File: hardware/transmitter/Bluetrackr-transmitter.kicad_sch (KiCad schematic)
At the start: 57 parts, among them J1 USB_C_Receptacle_USB2.0, J2 Programming_Connector, J3 Battery_Connector, Q1 CJ2333, Q2 BSS138, Q3 BSS138, Q4 BSS138, Q5 BSS138, Q6 BSS138, SW1 SW_Pair, U1 MCP73831-2-OT, U2 MIC5205-3.3YM5, U3 MCP1700-1802E_SOT23, U4 STM32F030R8Tx, U5 NRF24L01_Breakout, U6 ICM-20948

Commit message: Change level shifting resistors to 10k
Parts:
- R10, R11, R12, R13, R14, R15, R16, R17, R18, R19: value 2.2k -> 10k
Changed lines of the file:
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@@
   (junction (at 359.41 142.24))
   (junction (at 359.41 173.99))
+  (no_connect (at 217.17 148.59))
+  (no_connect (at 247.65 176.53))
+  (no_connect (at 217.17 186.69))
+  (no_connect (at 217.17 181.61))
+  (no_connect (at 54.61 73.66))
+  (no_connect (at 247.65 138.43))
+  (no_connect (at 217.17 194.31))
+  (no_connect (at 247.65 186.69))
+  (no_connect (at 54.61 60.96))
+  (no_connect (at 247.65 143.51))
+  (no_connect (at 325.12 57.15))
+  (no_connect (at 247.65 156.21))
+  (no_connect (at 217.17 196.85))
+  (no_connect (at 247.65 166.37))
+  (no_connect (at 247.65 140.97))
+  (no_connect (at 217.17 173.99))
+  (no_connect (at 217.17 168.91))
+  (no_connect (at 217.17 199.39))
+  (no_connect (at 247.65 148.59))
+  (no_connect (at 217.17 184.15))
   (no_connect (at 247.65 161.29))
+  (no_connect (at 325.12 54.61))
+  (no_connect (at 247.65 146.05))
+  (no_connect (at 217.17 138.43))
+  (no_connect (at 247.65 171.45))
+  (no_connect (at 217.17 179.07))
+  (no_connect (at 54.61 63.5))
+  (no_connect (at 217.17 156.21))
+  (no_connect (at 299.72 62.23))
+  (no_connect (at 217.17 143.51))
+  (no_connect (at 217.17 140.97))
+  (no_connect (at 247.65 184.15))
+  (no_connect (at 247.65 181.61))
+  (no_connect (at 247.65 168.91))
+  (no_connect (at 247.65 123.19))
+  (no_connect (at 247.65 179.07))
+  (no_connect (at 217.17 189.23))
+  (no_connect (at 54.61 58.42))
+  (no_connect (at 247.65 125.73))
+  (no_connect (at 247.65 173.99))
+  (no_connect (at 217.17 151.13))
+  (no_connect (at 247.65 163.83))
   (no_connect (at 217.17 191.77))
-  (no_connect (at 247.65 163.83))
-  (no_connect (at 299.72 62.23))
-  (no_connect (at 54.61 63.5))
-  (no_connect (at 247.65 156.21))
-  (no_connect (at 217.17 181.61))
-  (no_connect (at 247.65 184.15))
-  (no_connect (at 247.65 123.19))
-  (no_connect (at 54.61 60.96))
-  (no_connect (at 325.12 57.15))
-  (no_connect (at 217.17 140.97))
-  (no_connect (at 247.65 181.61))
-  (no_connect (at 217.17 184.15))
+  (no_connect (at 247.65 189.23))
   (no_connect (at 54.61 66.04))
-  (no_connect (at 247.65 166.37))
-  (no_connect (at 247.65 138.43))
-  (no_connect (at 247.65 143.51))
-  (no_connect (at 247.65 186.69))
-  (no_connect (at 247.65 140.97))
-  (no_connect (at 217.17 196.85))
-  (no_connect (at 54.61 73.66))
-  (no_connect (at 217.17 148.59))
-  (no_connect (at 217.17 186.69))
-  (no_connect (at 247.65 148.59))
-  (no_connect (at 217.17 156.21))
   (no_connect (at 54.61 76.2))
-  (no_connect (at 247.65 173.99))
-  (no_connect (at 247.65 176.53))
-  (no_connect (at 217.17 173.99))
-  (no_connect (at 217.17 199.39))
-  (no_connect (at 247.65 125.73))
-  (no_connect (at 247.65 171.45))
-  (no_connect (at 217.17 143.51))
-  (no_connect (at 217.17 189.23))
-  (no_connect (at 247.65 146.05))
-  (no_connect (at 217.17 179.07))
-  (no_connect (at 217.17 168.91))
-  (no_connect (at 247.65 189.23))
-  (no_connect (at 325.12 54.61))
-  (no_connect (at 217.17 138.43))
-  (no_connect (at 247.65 168.91))
-  (no_connect (at 247.65 179.07))
-  (no_connect (at 217.17 194.31))
-  (no_connect (at 54.61 58.42))
-  (no_connect (at 217.17 151.13))
   (wire (pts (xy 31.75 83.82) (xy 31.75 86.36))
     (stroke (width 0) (type solid) (color 0 0 0 0))
@@
       (effects (font (size 1.27 1.27)) (justify left))
     )
-    (property "Value" "2.2k" (id 1) (at 300.228 137.033 0)
+    (property "Value" "10k" (id 1) (at 300.228 137.033 0)
       (effects (font (size 1.27 1.27)) (justify left))
     )
@@
       (effects (font (size 1.27 1.27)) (justify left))
     )
-    (property "Value" "2.2k" (id 1) (at 300.228 168.783 0)
+    (property "Value" "10k" (id 1) (at 300.228 168.783 0)
       (effects (font (size 1.27 1.27)) (justify left))
     )
@@
       (effects (font (size 1.27 1.27)) (justify left))
     )
-    (property "Value" "2.2k" (id 1) (at 315.468 137.033 0)
+    (property "Value" "10k" (id 1) (at 315.468 137.033 0)
       (effects (font (size 1.27 1.27)) (justify left))
     )
@@
       (effects (font (size 1.27 1.27)) (justify left))
     )
-    (property "Value" "2.2k" (id 1) (at 315.468 168.783 0)
+    (property "Value" "10k" (id 1) (at 315.468 168.783 0)
       (effects (font (size 1.27 1.27)) (justify left))
     )
@@
       (effects (font (size 1.27 1.27)) (justify left))
     )
-    (property "Value" "2.2k" (id 1) (at 323.088 105.283 0)
+    (property "Value" "10k" (id 1) (at 323.088 105.283 0)
       (effects (font (size 1.27 1.27)) (justify left))
     )
@@
       (effects (font (size 1.27 1.27)) (justify left))
     )
-    (property "Value" "2.2k" (id 1) (at 338.328 105.283 0)
+    (property "Value" "10k" (id 1) (at 338.328 105.283 0)
       (effects (font (size 1.27 1.27)) (justify left))
     )
@@
       (effects (font (size 1.27 1.27)) (justify left))
     )
-    (property "Value" "2.2k" (id 1) (at 345.948 137.033 0)
+    (property "Value" "10k" (id 1) (at 345.948 137.033 0)
       (effects (font (size 1.27 1.27)) (justify left))
     )
@@
       (effects (font (size 1.27 1.27)) (justify left))
     )
-    (property "Value" "2.2k" (id 1) (at 345.948 168.783 0)
+    (property "Value" "10k" (id 1) (at 345.948 168.783 0)
       (effects (font (size 1.27 1.27)) (justify left))
     )
@@
       (effects (font (size 1.27 1.27)) (justify left))
     )
-    (property "Value" "2.2k" (id 1) (at 361.188 137.033 0)
+    (property "Value" "10k" (id 1) (at 361.188 137.033 0)
       (effects (font (size 1.27 1.27)) (justify left))
     )
@@
       (effects (font (size 1.27 1.27)) (justify left))
     )
-    (property "Value" "2.2k" (id 1) (at 361.188 168.783 0)
-      (effects (font (size 1.27 1.27)) (justify left))
-    )
+    (property "Value" "10k" (id 1) (at 361.188 168.783 0)
+      (effects (font (size 1.27 1.27)) (justify left))
+    )

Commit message: Changed regulator from 3.3V to 2.5V
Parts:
- removed U2: MIC5205-3.3YM5, Package_TO_SOT_SMD:SOT-23-5, symbol Regulator_Linear:MIC5205-3.3YM5
- added U?: MIC5205-2.5YM5, Package_TO_SOT_SMD:SOT-23-5, symbol Regulator_Linear:MIC5205-2.5YM5
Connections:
- net GND: now also U?.2 (GND)
- net VCC: now also U?.1 (IN), U?.3 (EN)
- net at C4.1: now also U?.4 (BP)
- net +3V3 renamed +2V5
- net +2V5: now also U?.5 (OUT)
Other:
- note added: "2.5V"
- note removed: "3.3V"

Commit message: Began routing the pcb
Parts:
- added C1, C3: 4.7u, Capacitor_SMD:C_0805_2012Metric_Pad1.15x1.40mm_HandSolder, symbol Device:C
- J2: footprint Connector_JST:JST_XH_S4B-XH-A_1x04_P2.50mm_Horizontal -> Connector_JST:JST_XH_B4B-XH-A_1x04_P2.50mm_Vertical
- J3: footprint Connector_JST:JST_XH_B2B-XH-A_1x02_P2.50mm_Vertical -> Connector_JST:JST_XH_S2B-XH-A_1x02_P2.50mm_Horizontal
- U5: footprint RF_Module:nRF24L01_Breakout -> Modules:nRF24L01_Breakout
- gave numbers to parts that had none: 1
- renumbered C8 to C10, C9 to C11, C10 to C12, C11 to C13, C12 to C14, C13 to C15, C14 to C16, C15 to C17, C1 to C2, C2 to C4, C3 to C5, C4 to C6, C5 to C7, C6 to C8, C7 to C9
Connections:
- net +BATT: now also C3.1
- net BATT_SENSE: now also U4.57 (PB5); no longer U4.14 (PA0)
- net GND: now also C1.2, C3.2
- net VBUS: now also C1.1
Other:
- moved on the sheet: C4, C5, C6, C7, C8, U2, U3

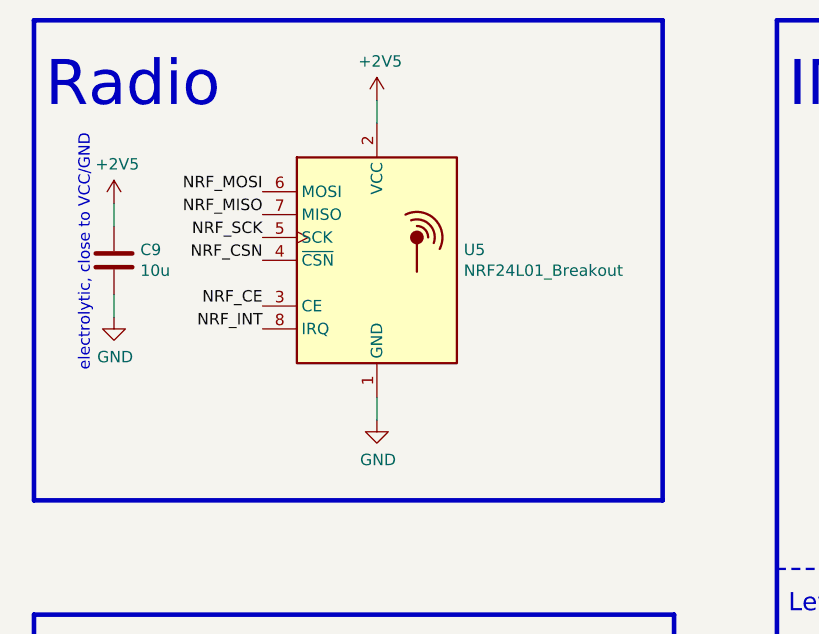
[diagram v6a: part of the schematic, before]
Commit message: Replace nRF24 breakout with DL-24N nRF24 smd module
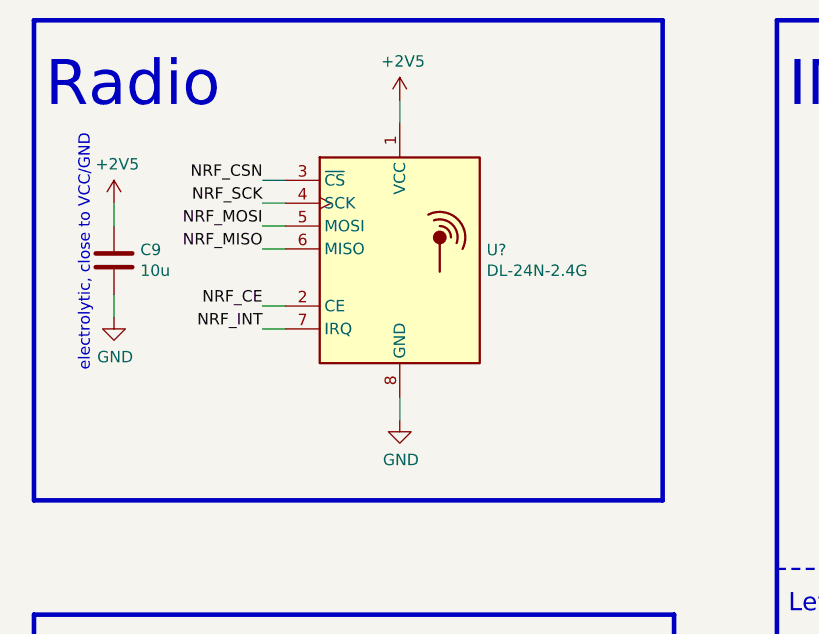
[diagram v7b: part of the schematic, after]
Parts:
- removed U5: NRF24L01_Breakout, Modules:nRF24L01_Breakout, symbol RF:NRF24L01_Breakout
- added U?: DL-24N-2.4G, User_Module:DL-24N-2.4G, symbol User_Module:DL-24N-2.4G
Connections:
- net +2V5: now also U?.1 (VCC)
- net GND: now also U?.8 (GND)
- net NRF_CE: now also U?.2 (CE)
- net NRF_CSN: now also U?.3 (~CS)
- net NRF_INT: now also U?.7 (IRQ)
- net NRF_MISO: now also U?.6 (MISO)
- net NRF_MOSI: now also U?.5 (MOSI)
- net NRF_SCK: now also U?.4 (SCK)
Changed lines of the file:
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@@
-(kicad_sch (version 20200602) (host eeschema "(5.99.0-1899-g8e8979e31)")
+(kicad_sch (version 20200602) (host eeschema "(5.99.0-1933-g2401ed587)")
   (page 1 1)
   (paper "A3")
@@
   (junction (at 359.41 142.24))
   (junction (at 359.41 173.99))
-  (no_connect (at 217.17 148.59))
-  (no_connect (at 54.61 66.04))
-  (no_connect (at 54.61 63.5))
-  (no_connect (at 54.61 60.96))
-  (no_connect (at 217.17 173.99))
-  (no_connect (at 325.12 54.61))
+  (no_connect (at 217.17 168.91))
+  (no_connect (at 325.12 57.15))
   (no_connect (at 247.65 166.37))
   (no_connect (at 217.17 196.85))
-  (no_connect (at 247.65 118.11))
-  (no_connect (at 217.17 199.39))
-  (no_connect (at 325.12 57.15))
+  (no_connect (at 247.65 140.97))
+  (no_connect (at 325.12 54.61))
+  (no_connect (at 54.61 60.96))
+  (no_connect (at 54.61 73.66))
   (no_connect (at 247.65 161.29))
-  (no_connect (at 217.17 191.77))
-  (no_connect (at 217.17 184.15))
+  (no_connect (at 247.65 184.15))
+  (no_connect (at 217.17 189.23))
   (no_connect (at 247.65 143.51))
-  (no_connect (at 247.65 163.83))
+  (no_connect (at 54.61 63.5))
+  (no_connect (at 217.17 156.21))
+  (no_connect (at 247.65 171.45))
   (no_connect (at 247.65 138.43))
-  (no_connect (at 247.65 123.19))
-  (no_connect (at 54.61 76.2))
-  (no_connect (at 247.65 184.15))
-  (no_connect (at 217.17 181.61))
-  (no_connect (at 54.61 58.42))
-  (no_connect (at 247.65 140.97))
   (no_connect (at 247.65 148.59))
-  (no_connect (at 217.17 138.43))
-  (no_connect (at 247.65 176.53))
-  (no_connect (at 299.72 62.23))
-  (no_connect (at 247.65 125.73))
-  (no_connect (at 247.65 168.91))
-  (no_connect (at 217.17 189.23))
+  (no_connect (at 217.17 194.31))
   (no_connect (at 247.65 146.05))
-  (no_connect (at 217.17 186.69))
-  (no_connect (at 247.65 171.45))
-  (no_connect (at 247.65 189.23))
-  (no_connect (at 217.17 168.91))
   (no_connect (at 247.65 179.07))
+  (no_connect (at 217.17 173.99))
+  (no_connect (at 299.72 62.23))
+  (no_connect (at 54.61 76.2))
+  (no_connect (at 217.17 140.97))
+  (no_connect (at 217.17 143.51))
+  (no_connect (at 217.17 199.39))
+  (no_connect (at 217.17 148.59))
+  (no_connect (at 247.65 176.53))
+  (no_connect (at 54.61 66.04))
+  (no_connect (at 247.65 189.23))
+  (no_connect (at 247.65 123.19))
+  (no_connect (at 217.17 191.77))
+  (no_connect (at 217.17 138.43))
+  (no_connect (at 217.17 181.61))
   (no_connect (at 217.17 179.07))
-  (no_connect (at 217.17 156.21))
-  (no_connect (at 247.65 156.21))
-  (no_connect (at 247.65 186.69))
+  (no_connect (at 247.65 118.11))
+  (no_connect (at 247.65 163.83))
+  (no_connect (at 217.17 184.15))
+  (no_connect (at 217.17 186.69))
   (no_connect (at 217.17 151.13))
+  (no_connect (at 247.65 168.91))
+  (no_connect (at 247.65 186.69))
   (no_connect (at 247.65 181.61))
-  (no_connect (at 217.17 140.97))
-  (no_connect (at 54.61 73.66))
-  (no_connect (at 217.17 143.51))
-  (no_connect (at 217.17 194.31))
+  (no_connect (at 54.61 58.42))
+  (no_connect (at 247.65 125.73))
+  (no_connect (at 247.65 156.21))
   (wire (pts (xy 31.75 83.82) (xy 31.75 86.36))
     (stroke (width 0) (type solid) (color 0 0 0 0))
@@
     (stroke (width 0) (type solid) (color 0 0 0 0))
   )
+  (wire (pts (xy 220.98 43.18) (xy 223.52 43.18))
+    (stroke (width 0) (type solid) (color 0 0 0 0))
+  )
+  (wire (pts (xy 220.98 45.72) (xy 223.52 45.72))
+    (stroke (width 0) (type solid) (color 0 0 0 0))
+  )
+  (wire (pts (xy 220.98 48.26) (xy 223.52 48.26))
+    (stroke (width 0) (type solid) (color 0 0 0 0))
+  )
+  (wire (pts (xy 220.98 50.8) (xy 223.52 50.8))
+    (stroke (width 0) (type solid) (color 0 0 0 0))
+  )
+  (wire (pts (xy 220.98 57.15) (xy 223.52 57.15))
+    (stroke (width 0) (type solid) (color 0 0 0 0))
+  )
+  (wire (pts (xy 220.98 59.69) (xy 223.52 59.69))
+    (stroke (width 0) (type solid) (color 0 0 0 0))
+  )
   (wire (pts (xy 229.87 107.95) (xy 229.87 110.49))
     (stroke (width 0) (type solid) (color 0 0 0 0))
@@
     (stroke (width 0) (type solid) (color 0 0 0 0))
   )
-  (wire (pts (xy 233.68 34.29) (xy 233.68 36.83))
-    (stroke (width 0) (type solid) (color 0 0 0 0))
-  )
-  (wire (pts (xy 233.68 67.31) (xy 233.68 69.85))
-    (stroke (width 0) (type solid) (color 0 0 0 0))
-  )
   (wire (pts (xy 234.95 110.49) (xy 232.41 110.49))
     (stroke (width 0) (type solid) (color 0 0 0 0))
@@
     (stroke (width 0) (type solid) (color 0 0 0 0))
   )
+  (wire (pts (xy 236.22 34.29) (xy 236.22 36.83))
+    (stroke (width 0) (type solid) (color 0 0 0 0))
+  )
+  (wire (pts (xy 236.22 67.31) (xy 236.22 69.85))
+    (stroke (width 0) (type solid) (color 0 0 0 0))
+  )
   (wire (pts (xy 237.49 110.49) (xy 234.95 110.49))
     (stroke (width 0) (type solid) (color 0 0 0 0))
@@
     (effects (font (size 1.27 1.27)) (justify right bottom))
   )
-  (label "NRF_MOSI" (at 220.98 44.45 180)
+  (label "NRF_CSN" (at 220.98 43.18 180)
     (effects (font (size 1.27 1.27)) (justify right bottom))
   )
-  (label "NRF_MISO" (at 220.98 46.99 180)
+  (label "NRF_SCK" (at 220.98 45.72 180)
     (effects (font (size 1.27 1.27)) (justify right bottom))
   )
-  (label "NRF_SCK" (at 220.98 49.53 180)
+  (label "NRF_MOSI" (at 220.98 48.26 180)
     (effects (font (size 1.27 1.27)) (justify right bottom))
   )
-  (label "NRF_CSN" (at 220.98 52.07 180)
+  (label "NRF_MISO" (at 220.98 50.8 180)
     (effects (font (size 1.27 1.27)) (justify right bottom))
   )
@@
     )
   )
-  (symbol (lib_id "power:+2V5") (at 233.68 34.29 0) (unit 1)
+  (symbol (lib_id "power:+2V5") (at 236.22 34.29 0) (unit 1)
     (in_bom yes)
-    (property "Reference" "#PWR042" (id 0) (at 233.68 38.1 0)
+    (property "Reference" "#PWR042" (id 0) (at 236.22 38.1 0)
       (effects (font (size 1.27 1.27)) hide)
     )
-    (property "Value" "+2V5" (id 1) (at 234.0483 29.9656 0))
-    (property "Footprint" "" (id 2) (at 233.68 34.29 0)
+    (property "Value" "+2V5" (id 1) (at 236.5883 29.9656 0))
+    (property "Footprint" "" (id 2) (at 236.22 34.29 0)
       (effects (font (size 1.27 1.27)) hide)
     )
-    (property "Datasheet" "" (id 3) (at 233.68 34.29 0)
+    (property "Datasheet" "" (id 3) (at 236.22 34.29 0)
       (effects (font (size 1.27 1.27)) hide)
     )
@@
     )
   )
-  (symbol (lib_id "power:GND") (at 233.68 69.85 0) (unit 1)
+  (symbol (lib_id "power:GND") (at 236.22 69.85 0) (unit 1)
     (in_bom yes)
-    (property "Reference" "#PWR043" (id 0) (at 233.68 76.2 0)
+    (property "Reference" "#PWR043" (id 0) (at 236.22 76.2 0)
       (effects (font (size 1.27 1.27)) hide)
     )
-    (property "Value" "GND" (id 1) (at 233.807 74.2442 0))
-    (property "Footprint" "" (id 2) (at 233.68 69.85 0)
+    (property "Value" "GND" (id 1) (at 236.347 74.2442 0))
+    (property "Footprint" "" (id 2) (at 236.22 69.85 0)
       (effects (font (size 1.27 1.27)) hide)
     )
-    (property "Datasheet" "" (id 3) (at 233.68 69.85 0)
+    (property "Datasheet" "" (id 3) (at 236.22 69.85 0)
       (effects (font (size 1.27 1.27)) hide)
     )
@@
     )
   )
-  (symbol (lib_id "RF:NRF24L01_Breakout") (at 233.68 52.07 0) (unit 1)
+  (symbol (lib_id "User_Module:DL-24N-2.4G") (at 236.22 52.07 0) (unit 1)
     (in_bom yes)
-    (property "Reference" "U5" (id 0) (at 243.332 50.9016 0)
+    (property "Reference" "U?" (id 0) (at 245.8721 50.9206 0)
       (effects (font (size 1.27 1.27)) (justify left))
     )
-    (property "Value" "NRF24L01_Breakout" (id 1) (at 243.332 53.213 0)
+    (property "Value" "DL-24N-2.4G" (id 1) (at 245.8721 53.2193 0)
       (effects (font (size 1.27 1.27)) (justify left))
     )
-    (property "Footprint" "Modules:nRF24L01_Breakout" (id 2) (at 237.49 36.83 0)
+    (property "Footprint" "User_Module:DL-24N-2.4G" (id 2) (at 237.49 36.83 0)
       (effects (font (size 1.27 1.27) italic) (justify left) hide)
     )
-    (property "Datasheet" "http://www.nordicsemi.com/eng/content/download/2730/34105/file/nRF24L01_Product_Specification_v2_0.pdf" (id 3) (at 233.68 54.61 0)
+    (property "Datasheet" "https://datasheet.lcsc.com/szlcsc/1912111437_DreamLNK-DL-24N-2-4G_C381181.pdf" (id 3) (at 236.22 53.34 0)
       (effects (font (size 1.27 1.27)) hide)
     )
@@
       (reference "U4") (unit 1)
     )
-    (path "/00000000-0000-0000-0000-00005f249c71"
-      (reference "U5") (unit 1)
-    )
     (path "/00000000-0000-0000-0000-00005f3e8d74"
       (reference "U6") (unit 1)
     )
+    (path "/625b9bb0-7ea4-4718-b98c-5a9c4e19210d"
+      (reference "U?") (unit 1)
+    )
   )
